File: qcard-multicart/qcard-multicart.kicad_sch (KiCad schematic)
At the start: 12 parts, among them J1 Conn_02x18_Top_Bottom, SW1 SW_DIP_x04, U1 MX29LV640EBTI-70G, U2 MIC5365-3.3YD5

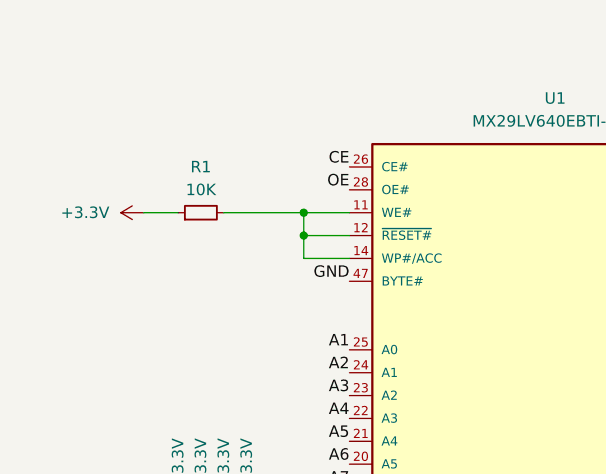
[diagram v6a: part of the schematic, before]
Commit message: Move all components to front
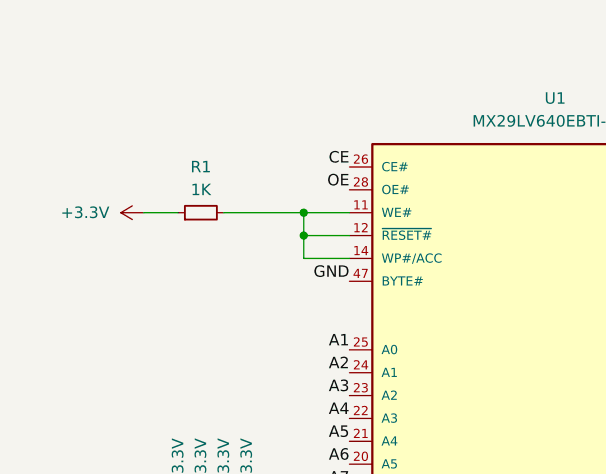
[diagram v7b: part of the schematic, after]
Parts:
- R1: value 10K -> 1K

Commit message: Production ready files
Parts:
- SW1: value SW_DIP_x04 -> 774-1954MST
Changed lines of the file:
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@@
       (effects (font (size 1.27 1.27)))
     )
-    (property "Value" "SW_DIP_x04" (at 85.09 107.95 0)
+    (property "Value" "774-1954MST" (at 85.09 107.95 0)
       (effects (font (size 1.27 1.27)))
     )
